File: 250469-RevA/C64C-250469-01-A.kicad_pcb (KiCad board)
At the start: 2 copper layers, 390.6 x 136.2 mm, 131 parts, among them J1 Conn_01x20_Male, J10 LED, J2 Conn_02x12_Edge, J3 Conn_02x6_Edge, J4 DIN-6, J5 DIN-8, J6 Conn_02x22_Edge_Female, J7 DIN-7, J8 DB9_Female, J9 DB9_Female, M1 RF_Modulator, Q1 2SD313, Q2 2SC1815, Q3 2SC1815, Q5 2SC1384, U1 6526A, U10 41464, U11 41464, U18 4066, U19 2114, U2 6526A, U20 8701, U21 4066, U22 7416, U23 74LS14, U3 74LS08, U4 23128, U5 2332, U6 8500, U7 8565R2, U8 251715-01, U9 8580R5, Y1 Crystal

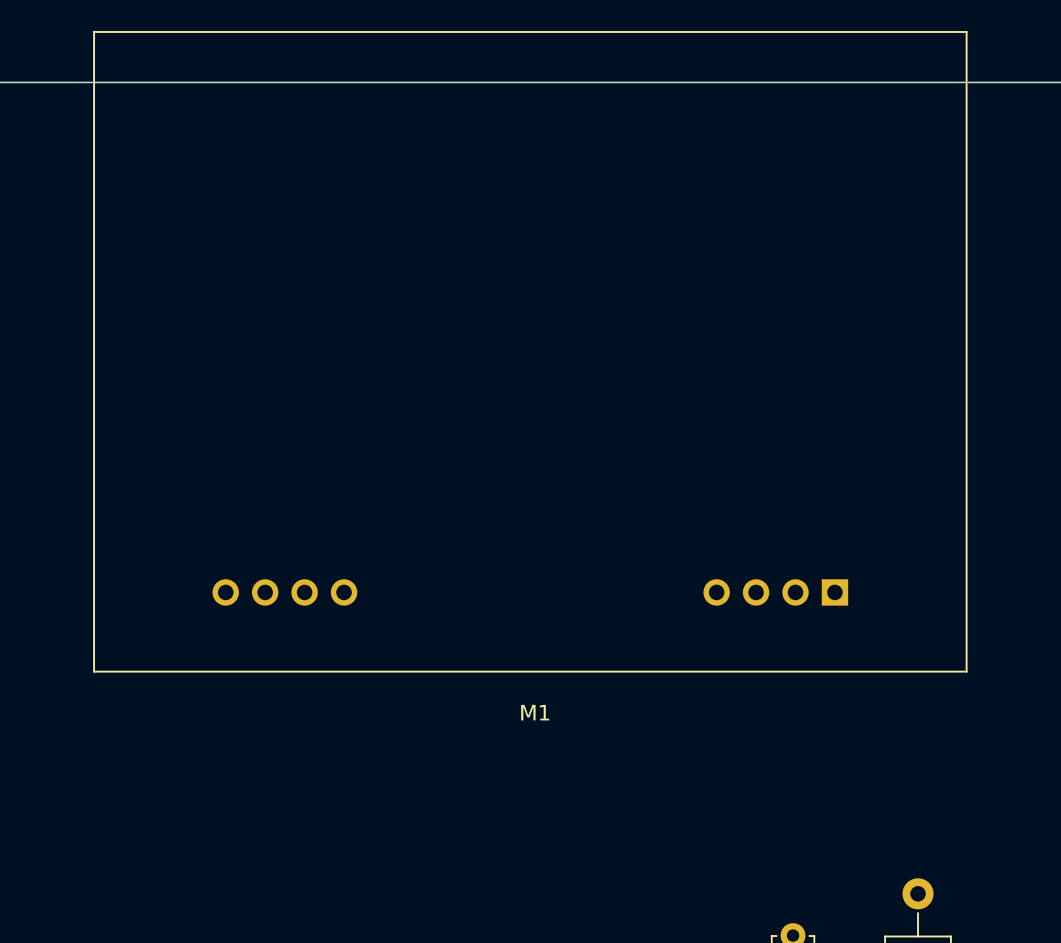
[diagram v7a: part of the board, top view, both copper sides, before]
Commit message: Fixed RF Modulator footprint and added 3D model
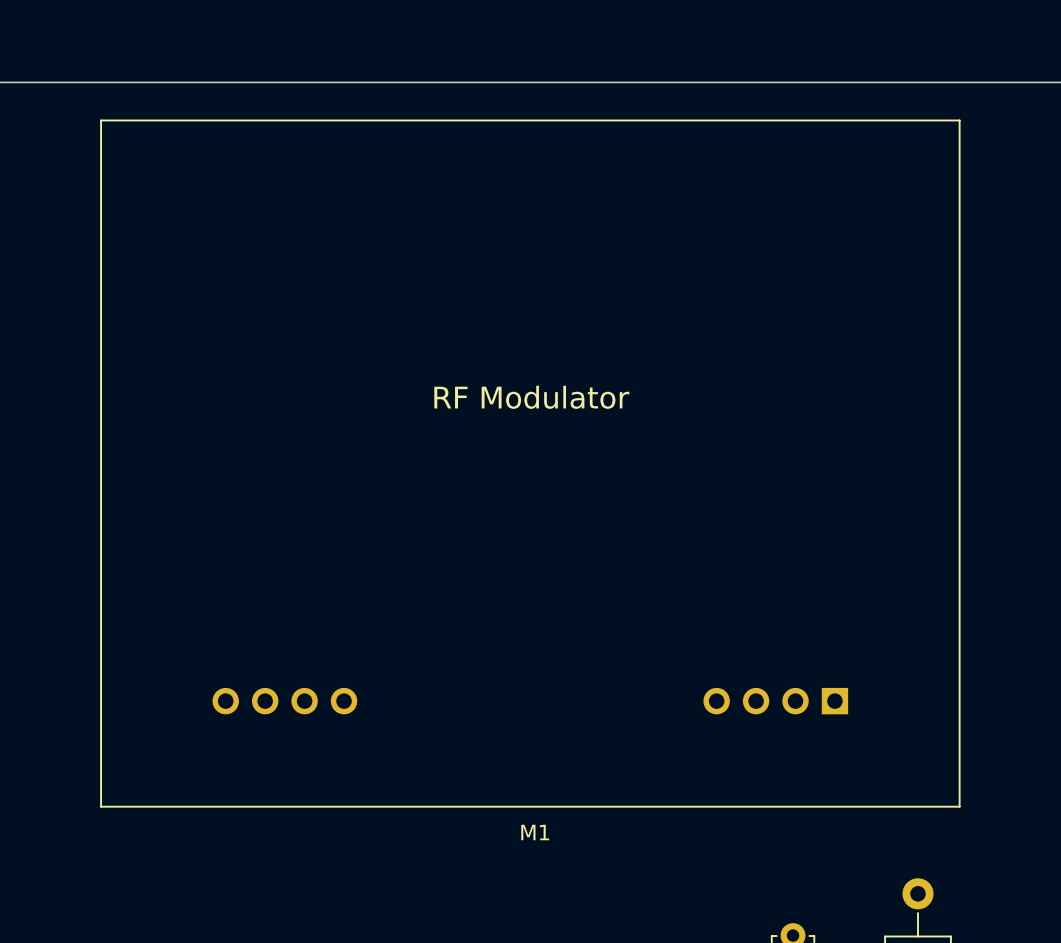
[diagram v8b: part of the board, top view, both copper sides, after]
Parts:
- moved M1 7.00 mm to (362.1, 169.4)
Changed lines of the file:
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@@
     (add_net ~VIC)
   )
+  (module 250469-01:RF_Modulator (layer F.Cu)
+    (at 362.1 169.45)
+    (fp_text reference M1 (at -19.31 8.5) (layer F.SilkS)
+      (effects (font (size 1 1) (thickness 0.15)))
+    )
+    (fp_text value RF_Modulator (at -19.62 -32.99) (layer F.Fab)
+      (effects (font (size 1 1) (thickness 0.15)))
+    )
+    (fp_text user "RF Modulator" (at -19.62 -19.5) (layer F.SilkS)
+      (effects (font (size 1.4 1.4) (thickness 0.2)))
+    )
+    (fp_text user %R (at -19.62 -15.5675) (layer F.Fab)
+      (effects (font (size 1 1) (thickness 0.15)))
+    )
+    (fp_line (start -47.12 6.7) (end 7.88 6.7) (layer F.Fab) (width 0.1))
+    (fp_line (start -47.12 -37.3) (end 7.88 -37.3) (layer F.Fab) (width 0.1))
+    (fp_line (start 7.88 6.7) (end 7.88 -37.3) (layer F.Fab) (width 0.1))
+    (fp_line (start -47.12 6.7) (end -47.12 -37.3) (layer F.Fab) (width 0.1))
+    (fp_line (start 8.03 6.8) (end 8.03 -37.4) (layer F.SilkS) (width 0.12))
+    (fp_line (start 8.03 -37.4) (end -47.27 -37.4) (layer F.SilkS) (width 0.12))
+    (fp_line (start -47.27 -37.4) (end -47.27 6.8) (layer F.SilkS) (width 0.12))
+    (fp_line (start -47.27 6.8) (end 8.03 6.8) (layer F.SilkS) (width 0.12))
+    (fp_line (start 10 9) (end 10 -38.4) (layer F.CrtYd) (width 0.05))
+    (fp_line (start 10 -38.4) (end -49.2 -38.4) (layer F.CrtYd) (width 0.05))
+    (fp_line (start -49.2 -38.4) (end -49.2 9) (layer F.CrtYd) (width 0.05))
+    (fp_line (start -49.2 9) (end 10 9) (layer F.CrtYd) (width 0.05))
+    (pad 8 thru_hole oval (at -39.24 0 270) (size 1.7 1.7) (drill 1) (layers *.Cu *.Mask)
+      (net 23 AUDIO_OUT))
+    (pad 7 thru_hole oval (at -36.7 0 270) (size 1.7 1.7) (drill 1) (layers *.Cu *.Mask)
+      (net 47 "Net-(FB2-Pad2)"))
+    (pad 6 thru_hole oval (at -34.16 0 270) (size 1.7 1.7) (drill 1) (layers *.Cu *.Mask)
+      (net 50 "Net-(FB3-Pad2)"))
+    (pad 5 thru_hole oval (at -31.62 0 270) (size 1.7 1.7) (drill 1) (layers *.Cu *.Mask)
+      (net 52 "Net-(FB4-Pad2)"))
+    (pad 1 thru_hole rect (at 0 0 270) (size 1.7 1.7) (drill 1) (layers *.Cu *.Mask)
+      (net 119 "Net-(L2-Pad2)"))
+    (pad 2 thru_hole oval (at -2.54 0 270) (size 1.7 1.7) (drill 1) (layers *.Cu *.Mask)
+      (net 122 "/Video - ClockGen/SL"))
+    (pad 3 thru_hole oval (at -5.08 0 270) (size 1.7 1.7) (drill 1) (layers *.Cu *.Mask)
+      (net 2 GND))
+    (pad 4 thru_hole oval (at -7.62 0 270) (size 1.7 1.7) (drill 1) (layers *.Cu *.Mask)
+      (net 121 "/Video - ClockGen/COLOR"))
+    (model ${KIPRJMOD}/../libs/250469-01.3dshapes/RF_Modulator.wrl
+      (at (xyz 0 0 0))
+      (scale (xyz 1 1 1))
+      (rotate (xyz 0 0 0))
+    )
+  )
   (module Package_DIP:DIP-40_W15.24mm_Socket (layer F.Cu)
     (at 361.3 206.75)
@@
       (effects (font (size 1 1) (thickness 0.15)))
     )
+    (fp_line (start 0.74 1.85) (end 4.34 1.85) (layer F.SilkS) (width 0.12))
+    (fp_line (start 0.8 1.75) (end 4.3 1.75) (layer F.Fab) (width 0.1))
+    (fp_line (start -1.01 -2.73) (end 6.09 -2.73) (layer F.CrtYd) (width 0.05))
+    (fp_line (start -1.01 -2.73) (end -1.01 2.01) (layer F.CrtYd) (width 0.05))
+    (fp_line (start 6.09 2.01) (end 6.09 -2.73) (layer F.CrtYd) (width 0.05))
+    (fp_line (start 6.09 2.01) (end -1.01 2.01) (layer F.CrtYd) (width 0.05))
     (fp_arc (start 2.54 0) (end 4.34 1.85) (angle -20) (layer F.SilkS) (width 0.12))
     (fp_arc (start 2.54 0) (end 2.54 -2.48) (angle -135) (layer F.Fab) (width 0.1))
@@
       (effects (font (size 1 1) (thickness 0.15)))
     )
-    (fp_line (start 0.74 1.85) (end 4.34 1.85) (layer F.SilkS) (width 0.12))
-    (fp_line (start 0.8 1.75) (end 4.3 1.75) (layer F.Fab) (width 0.1))
-    (fp_line (start -1.01 -2.73) (end 6.09 -2.73) (layer F.CrtYd) (width 0.05))
-    (fp_line (start -1.01 -2.73) (end -1.01 2.01) (layer F.CrtYd) (width 0.05))
-    (fp_line (start 6.09 2.01) (end 6.09 -2.73) (layer F.CrtYd) (width 0.05))
-    (fp_line (start 6.09 2.01) (end -1.01 2.01) (layer F.CrtYd) (width 0.05))
     (pad 1 thru_hole rect (at 0 0 90) (size 1.5 1.5) (drill 0.8) (layers *.Cu *.Mask)
       (net 9 +9V))
@@
       (at (xyz 0 0 0))
       (scale (xyz 1 1 1))
-      (rotate (xyz 0 0 0))
-    )
-  )
-  (module 250469-01:RF_Modulator (layer F.Cu)
-    (at 362.1 162.45)
-    (fp_text reference M1 (at -19.31 7.78) (layer F.SilkS)
-      (effects (font (size 1 1) (thickness 0.15)))
-    )
-    (fp_text value RF_Modulator (at -19.62 -33.99) (layer F.Fab)
-      (effects (font (size 1 1) (thickness 0.15)))
-    )
-    (fp_line (start -50.62 8) (end 11.38 8) (layer F.CrtYd) (width 0.05))
-    (fp_line (start -50.62 -38) (end -50.62 8) (layer F.CrtYd) (width 0.05))
-    (fp_line (start 11.38 -38) (end -50.62 -38) (layer F.CrtYd) (width 0.05))
-    (fp_line (start 11.38 8) (end 11.38 -38) (layer F.CrtYd) (width 0.05))
-    (fp_line (start -47.72 5.1) (end 8.48 5.1) (layer F.SilkS) (width 0.12))
-    (fp_line (start -47.72 -36.1) (end -47.72 5.1) (layer F.SilkS) (width 0.12))
-    (fp_line (start 8.48 -36.1) (end -47.72 -36.1) (layer F.SilkS) (width 0.12))
-    (fp_line (start 8.48 5.1) (end 8.48 -36.1) (layer F.SilkS) (width 0.12))
-    (fp_line (start -47.62 5) (end -47.62 -36) (layer F.Fab) (width 0.1))
-    (fp_line (start 8.38 5) (end 8.38 -36) (layer F.Fab) (width 0.1))
-    (fp_line (start -47.62 -36) (end 8.38 -36) (layer F.Fab) (width 0.1))
-    (fp_line (start -47.62 5) (end 8.38 5) (layer F.Fab) (width 0.1))
-    (fp_text user "WARNING: external measures are not precise" (at -19.62 -23.84) (layer Dwgs.User)
-      (effects (font (size 1 1) (thickness 0.15)))
-    )
-    (fp_text user %R (at -19.62 -15.5675) (layer F.Fab)
-      (effects (font (size 1 1) (thickness 0.15)))
-    )
-    (pad 8 thru_hole oval (at -39.24 0 270) (size 1.7 1.7) (drill 1) (layers *.Cu *.Mask)
-      (net 23 AUDIO_OUT))
-    (pad 7 thru_hole oval (at -36.7 0 270) (size 1.7 1.7) (drill 1) (layers *.Cu *.Mask)
-      (net 47 "Net-(FB2-Pad2)"))
-    (pad 6 thru_hole oval (at -34.16 0 270) (size 1.7 1.7) (drill 1) (layers *.Cu *.Mask)
-      (net 50 "Net-(FB3-Pad2)"))
-    (pad 5 thru_hole oval (at -31.62 0 270) (size 1.7 1.7) (drill 1) (layers *.Cu *.Mask)
-      (net 52 "Net-(FB4-Pad2)"))
-    (pad 1 thru_hole rect (at 0 0 270) (size 1.7 1.7) (drill 1) (layers *.Cu *.Mask)
-      (net 119 "Net-(L2-Pad2)"))
-    (pad 2 thru_hole oval (at -2.54 0 270) (size 1.7 1.7) (drill 1) (layers *.Cu *.Mask)
-      (net 122 "/Video - ClockGen/SL"))
-    (pad 3 thru_hole oval (at -5.08 0 270) (size 1.7 1.7) (drill 1) (layers *.Cu *.Mask)
-      (net 2 GND))
-    (pad 4 thru_hole oval (at -7.62 0 270) (size 1.7 1.7) (drill 1) (layers *.Cu *.Mask)
-      (net 121 "/Video - ClockGen/COLOR"))
-    (model ${KISYS3DMOD}/Connector_PinHeader_2.54mm.3dshapes/PinHeader_1x04_P2.54mm_Vertical.wrl
-      (at (xyz 0 0 0))
-      (scale (xyz 1 1 1))
